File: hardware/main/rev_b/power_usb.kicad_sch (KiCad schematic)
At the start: 32 parts, among them J1 USB-C USB2, J2 ESC_CAN_POWER, U1 USBLC6-2SC6, U2 TLV62569DBVR, U3 TLV75528PDBVR, U4 TLV75533PDBVR

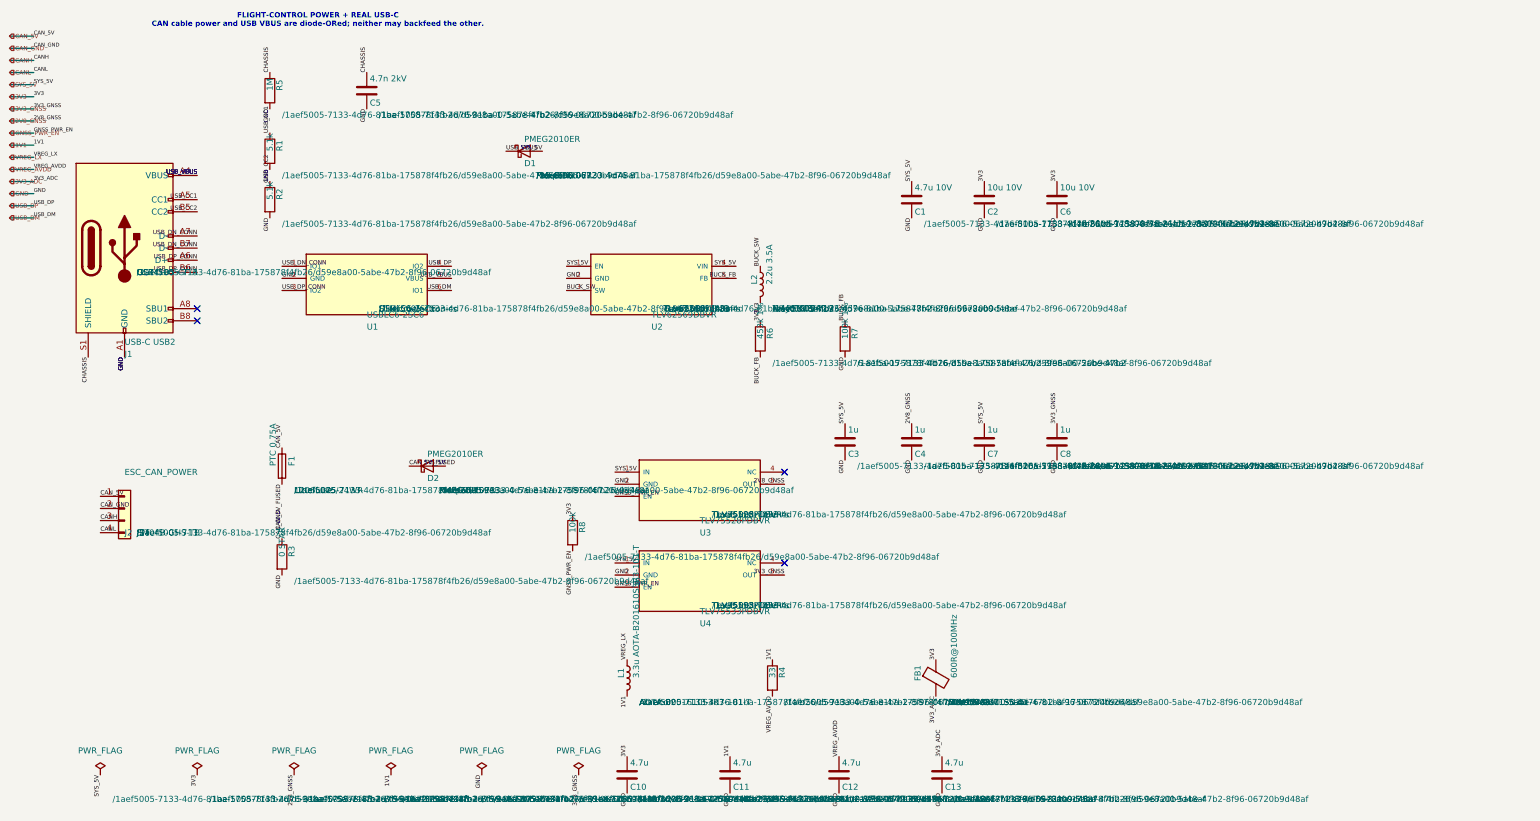
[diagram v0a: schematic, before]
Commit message: fix: consolidate portable Rev-B hardware sources
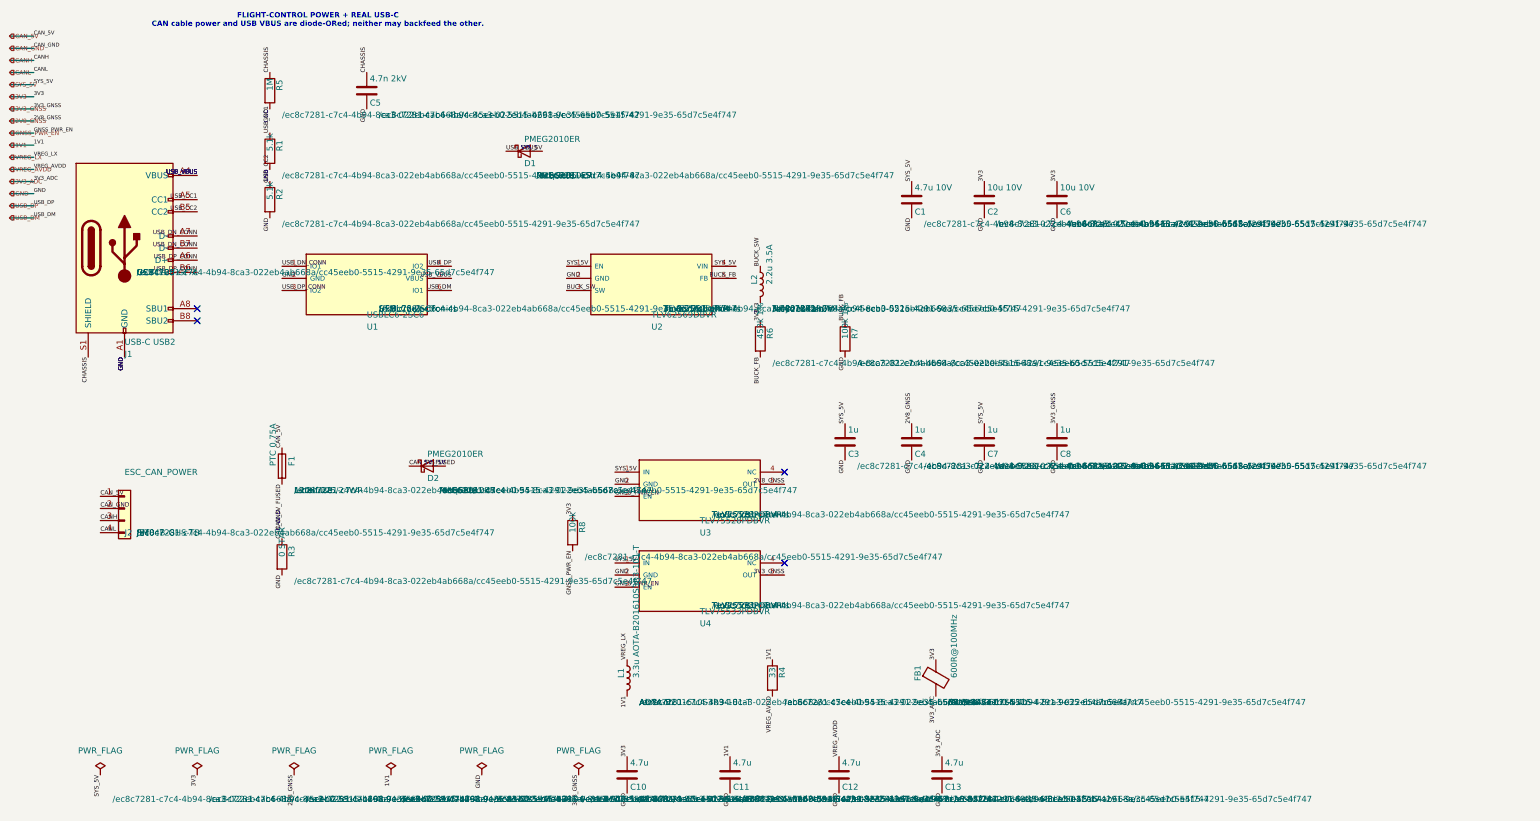
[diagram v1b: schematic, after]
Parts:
- C1, C10, C11, C12, C13, C2, C3, C4, C5, C6, C7, C8, D1, D2, F1, FB1, J1, J2, L1, L2, R1, R2, R3, R4, R5, R6, R7, R8, U1, U2, U3, U4: hierarchy_path /1aef5005-7133-4d76-81ba-175878f4fb26/d59e8a00-5abe-47b2-8f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 -> /ec8c7281-c7c4-4b94-8ca3-022eb4ab668a/cc45eeb0-5515-4291-9e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
